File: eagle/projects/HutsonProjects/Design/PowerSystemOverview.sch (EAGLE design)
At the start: 28 parts, among them U1 MCP7384XX, U3 MT3608, U4 LTC3531ES6-3_3

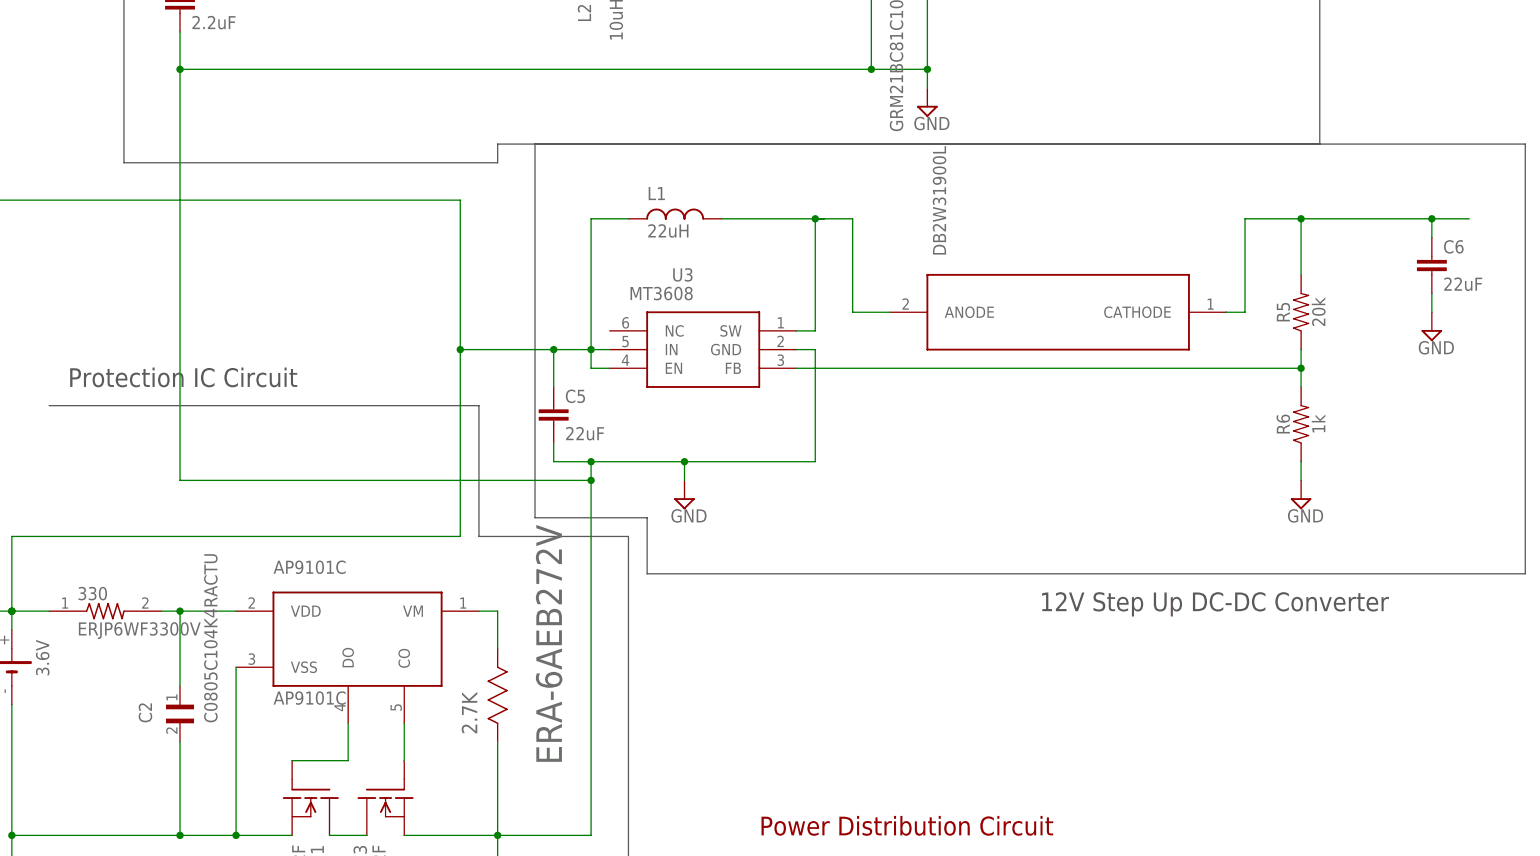
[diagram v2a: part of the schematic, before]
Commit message: 22 uf chip capacitor created
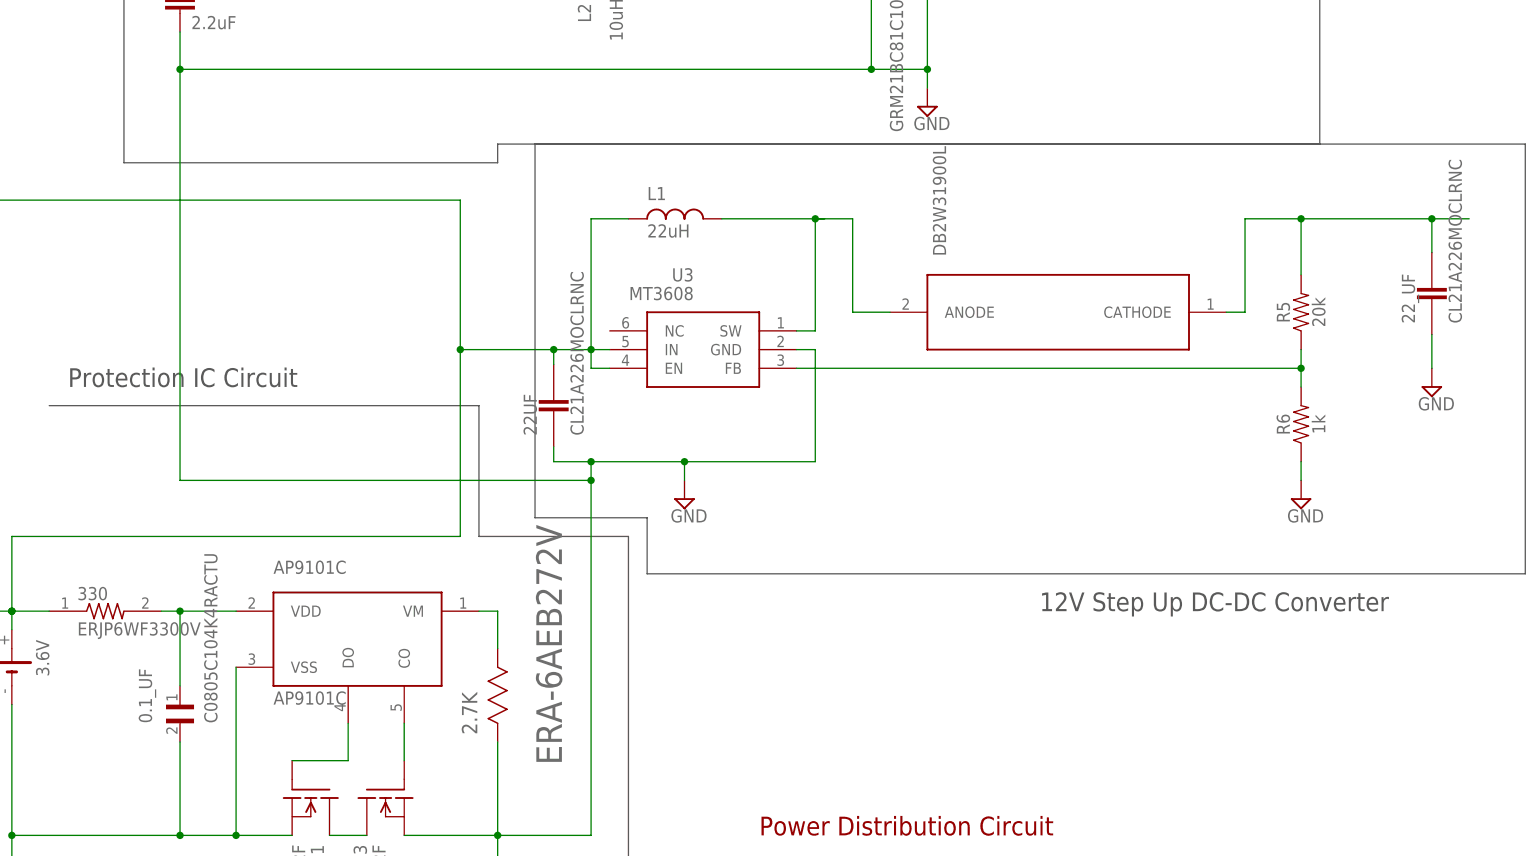
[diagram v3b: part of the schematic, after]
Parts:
- removed C5, C6: 22uF, SparkFun-Capacitors:22UF-0805-6.3V-20%
- added 22UF, 22_UF: CL21A226MOCLRNC, CL21A226MOCLRNC:CL21A226MOCLRNC
- renumbered C2 to 0.1_UF
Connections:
- net GND: now also 22UF.1, 22_UF.1; no longer C5.2, C6.2
- net N$16: now also 22UF.2; no longer C5.1
- net N$17: now also 22_UF.2; no longer C6.1
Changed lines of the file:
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@@
 <part name="SUPPLY5" library="supply2" library_urn="urn:adsk.eagle:library:372" deviceset="GND" device=""/>
 <part name="U3" library="MT3608" deviceset="MT3608" device=""/>
-<part name="C5" library="SparkFun-Capacitors" deviceset="22UF" device="-0805-6.3V-20%" value="22uF"/>
-<part name="C6" library="SparkFun-Capacitors" deviceset="22UF" device="-0805-6.3V-20%" value="22uF"/>
 <part name="L1" library="ngspice-simulation" library_urn="urn:adsk.eagle:library:527439" deviceset="L" device="" value="22uH"/>
 <part name="R5" library="SparkFun-Resistors" deviceset="20KOHM" device="-0603-1/10W-1%" value="20k"/>
 <part name="R6" library="SparkFun-Resistors" deviceset="1KOHM" device="-0603-1/10W-1%" value="1k"/>
 <part name="SUPPLY4" library="supply2" library_urn="urn:adsk.eagle:library:372" deviceset="GND" device=""/>
-<part name="SUPPLY7" library="supply2" library_urn="urn:adsk.eagle:library:372" deviceset="GND" device=""/>
 <part name="SUPPLY8" library="supply2" library_urn="urn:adsk.eagle:library:372" deviceset="GND" device=""/>
 <part name="SUPPLY14" library="supply2" library_urn="urn:adsk.eagle:library:372" deviceset="GND" device=""/>
@@
 <part name="10_UF" library="GRM21BC81C106KE15L" deviceset="GRM21BC81C106KE15L" device=""/>
 <part name="0.1UF" library="C0805C104K4RACTU" deviceset="C0805C104K4RACTU" device=""/>
-<part name="C2" library="C0805C104K4RACTU" deviceset="C0805C104K4RACTU" device=""/>
+<part name="0.1_UF" library="C0805C104K4RACTU" deviceset="C0805C104K4RACTU" device=""/>
+<part name="22UF" library="CL21A226MOCLRNC" deviceset="CL21A226MOCLRNC" device=""/>
+<part name="22_UF" library="CL21A226MOCLRNC" deviceset="CL21A226MOCLRNC" device=""/>
+<part name="SUPPLY7" library="supply2" library_urn="urn:adsk.eagle:library:372" deviceset="GND" device=""/>
 </parts>
 <sheets>
@@
 <attribute name="VALUE" x="181.61" y="154.94" size="1.778" layer="96" rot="MR0" align="center-left"/>
 </instance>
-<instance part="C5" gate="G$1" x="162.56" y="137.16" smashed="yes">
-<attribute name="NAME" x="164.084" y="140.081" size="1.778" layer="95" font="vector"/>
-<attribute name="VALUE" x="164.084" y="135.001" size="1.778" layer="96" font="vector"/>
-</instance>
-<instance part="C6" gate="G$1" x="281.94" y="157.48" smashed="yes">
-<attribute name="NAME" x="283.464" y="160.401" size="1.778" layer="95" font="vector"/>
-<attribute name="VALUE" x="283.464" y="155.321" size="1.778" layer="96" font="vector"/>
-</instance>
 <instance part="L1" gate="G$1" x="177.8" y="165.1" smashed="yes">
 <attribute name="NAME" x="175.26" y="167.64" size="1.778" layer="95"/>
@@
 <instance part="SUPPLY4" gate="GND" x="180.34" y="127" smashed="yes">
 <attribute name="VALUE" x="178.435" y="123.825" size="1.778" layer="96"/>
-</instance>
-<instance part="SUPPLY7" gate="GND" x="281.94" y="149.86" smashed="yes">
-<attribute name="VALUE" x="280.035" y="146.685" size="1.778" layer="96"/>
 </instance>
 <instance part="SUPPLY8" gate="GND" x="264.16" y="127" smashed="yes">
@@
 <attribute name="VALUE" x="63.5" y="78.74" size="1.778" layer="96" rot="R90"/>
 </instance>
-<instance part="C2" gate="G$1" x="111.76" y="96.52" smashed="yes" rot="R90">
+<instance part="0.1_UF" gate="G$1" x="111.76" y="96.52" smashed="yes" rot="R90">
 <attribute name="NAME" x="107.95" y="96.52" size="1.778" layer="95" rot="R90"/>
 <attribute name="VALUE" x="116.84" y="96.52" size="1.778" layer="96" rot="R90"/>
+</instance>
+<instance part="22UF" gate="G$1" x="162.56" y="139.7" smashed="yes" rot="R90">
+<attribute name="NAME" x="160.26521875" y="135.620390625" size="1.78483125" layer="95" rot="R90"/>
+<attribute name="VALUE" x="166.63265" y="135.62735" size="1.78178125" layer="96" rot="R90"/>
+</instance>
+<instance part="22_UF" gate="G$1" x="281.94" y="154.94" smashed="yes" rot="R90">
+<attribute name="NAME" x="279.64521875" y="150.860390625" size="1.78483125" layer="95" rot="R90"/>
+<attribute name="VALUE" x="286.01265" y="150.86735" size="1.78178125" layer="96" rot="R90"/>
+</instance>
+<instance part="SUPPLY7" gate="GND" x="281.94" y="142.24" smashed="yes">
+<attribute name="VALUE" x="280.035" y="139.065" size="1.778" layer="96"/>
 </instance>
 </instances>
@@
 </segment>
 <segment>
-<pinref part="C6" gate="G$1" pin="2"/>
-<pinref part="SUPPLY7" gate="GND" pin="GND"/>
-<wire x1="281.94" y1="154.94" x2="281.94" y2="152.4" width="0.1524" layer="91"/>
-</segment>
-<segment>
 <pinref part="R6" gate="G$1" pin="1"/>
 <pinref part="SUPPLY8" gate="GND" pin="GND"/>
@@
 <wire x1="119.38" y1="104.14" x2="119.38" y2="81.28" width="0.1524" layer="91"/>
 <junction x="119.38" y="81.28"/>
-<pinref part="C2" gate="G$1" pin="2"/>
+<pinref part="0.1_UF" gate="G$1" pin="2"/>
 <wire x1="111.76" y1="93.98" x2="111.76" y2="81.28" width="0.1524" layer="91"/>
 <junction x="111.76" y="81.28"/>
@@
 <junction x="154.94" y="81.28"/>
 <wire x1="154.94" y1="81.28" x2="167.64" y2="81.28" width="0.1524" layer="91"/>
-<pinref part="C5" gate="G$1" pin="2"/>
-<wire x1="162.56" y1="134.62" x2="162.56" y2="132.08" width="0.1524" layer="91"/>
 <wire x1="162.56" y1="132.08" x2="167.64" y2="132.08" width="0.1524" layer="91"/>
 <wire x1="167.64" y1="132.08" x2="180.34" y2="132.08" width="0.1524" layer="91"/>
@@
 <wire x1="213.36" y1="198.12" x2="213.36" y2="185.42" width="0.1524" layer="91"/>
 <junction x="213.36" y="185.42"/>
+<pinref part="22UF" gate="G$1" pin="1"/>
+<wire x1="162.56" y1="134.112" x2="162.56" y2="132.08" width="0.1524" layer="91"/>
 </segment>
 <segment>
@@
 <pinref part="SUPPLY2" gate="GND" pin="GND"/>
 <wire x1="58.42" y1="76.2" x2="58.42" y2="73.66" width="0.1524" layer="91"/>
+</segment>
+<segment>
+<pinref part="22_UF" gate="G$1" pin="1"/>
+<pinref part="SUPPLY7" gate="GND" pin="GND"/>
+<wire x1="281.94" y1="149.352" x2="281.94" y2="144.78" width="0.1524" layer="91"/>
 </segment>
 </net>
@@
 <wire x1="109.22" y1="111.76" x2="111.76" y2="111.76" width="0.1524" layer="91"/>
 <pinref part="330" gate="G$1" pin="2"/>
-<pinref part="C2" gate="G$1" pin="1"/>
+<pinref part="0.1_UF" gate="G$1" pin="1"/>
 <wire x1="111.76" y1="111.76" x2="119.38" y2="111.76" width="0.1524" layer="91"/>
 <wire x1="111.76" y1="101.6" x2="111.76" y2="111.76" width="0.1524" layer="91"/>
@@
 <wire x1="88.9" y1="111.76" x2="88.9" y2="121.92" width="0.1524" layer="91"/>
 <wire x1="88.9" y1="121.92" x2="149.86" y2="121.92" width="0.1524" layer="91"/>
-<pinref part="C5" gate="G$1" pin="1"/>
 <pinref part="L1" gate="G$1" pin="1"/>
 <wire x1="167.64" y1="165.1" x2="172.72" y2="165.1" width="0.1524" layer="91"/>
@@
 <junction x="167.64" y="147.32"/>
 <wire x1="167.64" y1="147.32" x2="167.64" y2="165.1" width="0.1524" layer="91"/>
+<wire x1="149.86" y1="147.32" x2="162.56" y2="147.32" width="0.1524" layer="91"/>
 <wire x1="162.56" y1="147.32" x2="167.64" y2="147.32" width="0.1524" layer="91"/>
-<wire x1="162.56" y1="147.32" x2="162.56" y2="142.24" width="0.1524" layer="91"/>
-<junction x="162.56" y="147.32"/>
-<wire x1="149.86" y1="147.32" x2="162.56" y2="147.32" width="0.1524" layer="91"/>
 <wire x1="149.86" y1="121.92" x2="149.86" y2="147.32" width="0.1524" layer="91"/>
 <wire x1="81.28" y1="111.76" x2="88.9" y2="111.76" width="0.1524" layer="91"/>
@@
 <wire x1="76.2" y1="91.44" x2="76.2" y2="86.36" width="0.1524" layer="91"/>
 <junction x="76.2" y="91.44"/>
+<pinref part="22UF" gate="G$1" pin="2"/>
+<wire x1="162.56" y1="147.32" x2="162.56" y2="145.288" width="0.1524" layer="91"/>
+<junction x="162.56" y="147.32"/>
 </segment>
 </net>
@@
 <pinref part="R5" gate="G$1" pin="2"/>
 <wire x1="264.16" y1="165.1" x2="264.16" y2="157.48" width="0.1524" layer="91"/>
-<pinref part="C6" gate="G$1" pin="1"/>
 <wire x1="264.16" y1="165.1" x2="281.94" y2="165.1" width="0.1524" layer="91"/>
-<wire x1="281.94" y1="165.1" x2="281.94" y2="162.56" width="0.1524" layer="91"/>
+<pinref part="U$6" gate="G$1" pin="CATHODE"/>
 <wire x1="281.94" y1="165.1" x2="287.02" y2="165.1" width="0.1524" layer="91"/>
-<junction x="281.94" y="165.1"/>
-<pinref part="U$6" gate="G$1" pin="CATHODE"/>
 <wire x1="254" y1="152.4" x2="256.54" y2="152.4" width="0.1524" layer="91"/>
 <wire x1="256.54" y1="152.4" x2="256.54" y2="165.1" width="0.1524" layer="91"/>
 <wire x1="256.54" y1="165.1" x2="264.16" y2="165.1" width="0.1524" layer="91"/>
 <junction x="264.16" y="165.1"/>
-</segment>
-</net>
+<pinref part="22_UF" gate="G$1" pin="2"/>
+<wire x1="281.94" y1="165.1" x2="281.94" y2="160.528" width="0.1524" layer="91"/>
+<junction x="281.94" y="165.1"/>
+</segment>
+</net>
